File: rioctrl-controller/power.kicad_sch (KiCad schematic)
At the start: 60 parts, among them J1 TERM-BLK-2H, U1 TD6811, U2 TPS54335ADDAR, U3 TPS54335ADDAR, U4 NCP114ASN250T1G

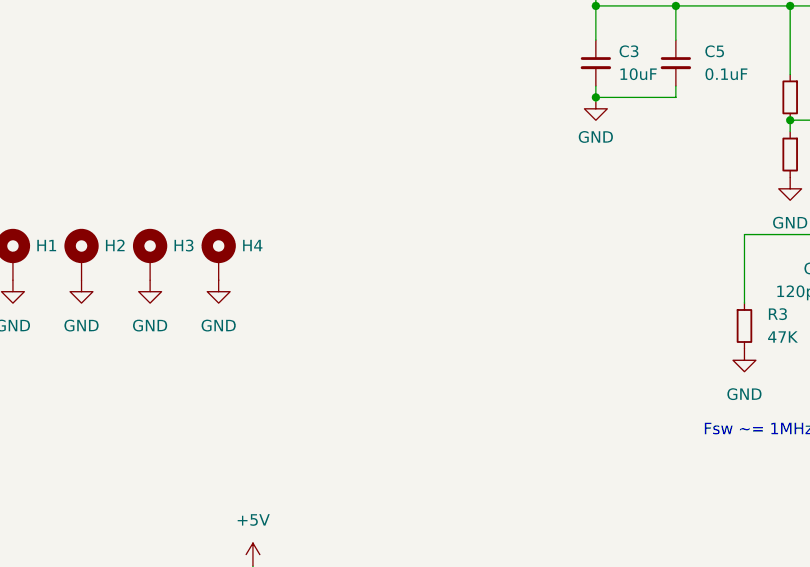
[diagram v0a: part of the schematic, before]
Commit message: Ditch the separate backplane board, increase the slot bitwidth to 12
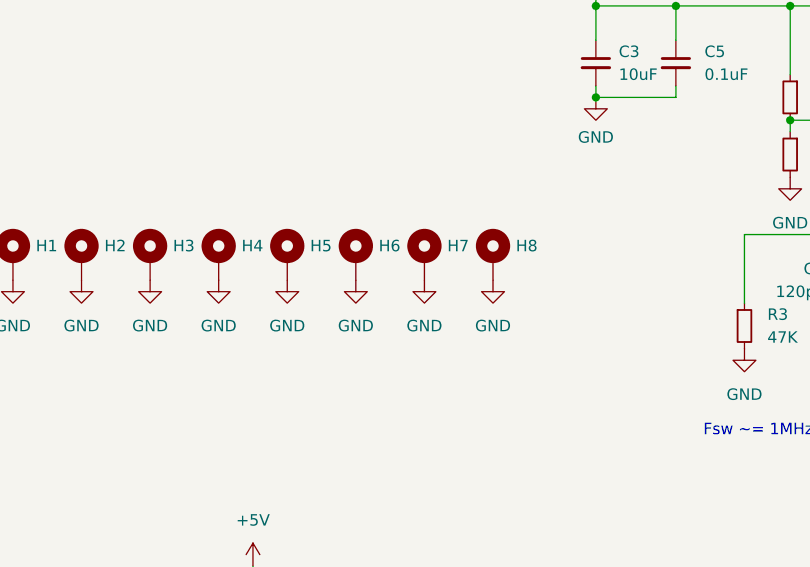
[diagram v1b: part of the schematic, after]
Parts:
- added H5, H6, H7, H8: MH_3.2mm, MountingHole:MountingHole_3.2mm_M3_Pad_Via, symbol hadv-mechanical:MH_3.2mm
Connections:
- net GND: now also H5.1, H6.1, H7.1, H8.1

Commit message: Fix ERC, add title information to sch, add initial version of build scripts
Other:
- company: (none) -> R. Veips
- title: (none) -> ${PROJECTNAME}
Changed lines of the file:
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@@
 	(generator_version "8.0")
 	(paper "A4")
+	(title_block
+		(title "${PROJECTNAME}")
+		(date "2024-08-25")
+		(rev "${VERSION}")
+		(company "R. Veips")
+	)
 	(junction
 		(at 45.72 29.21)

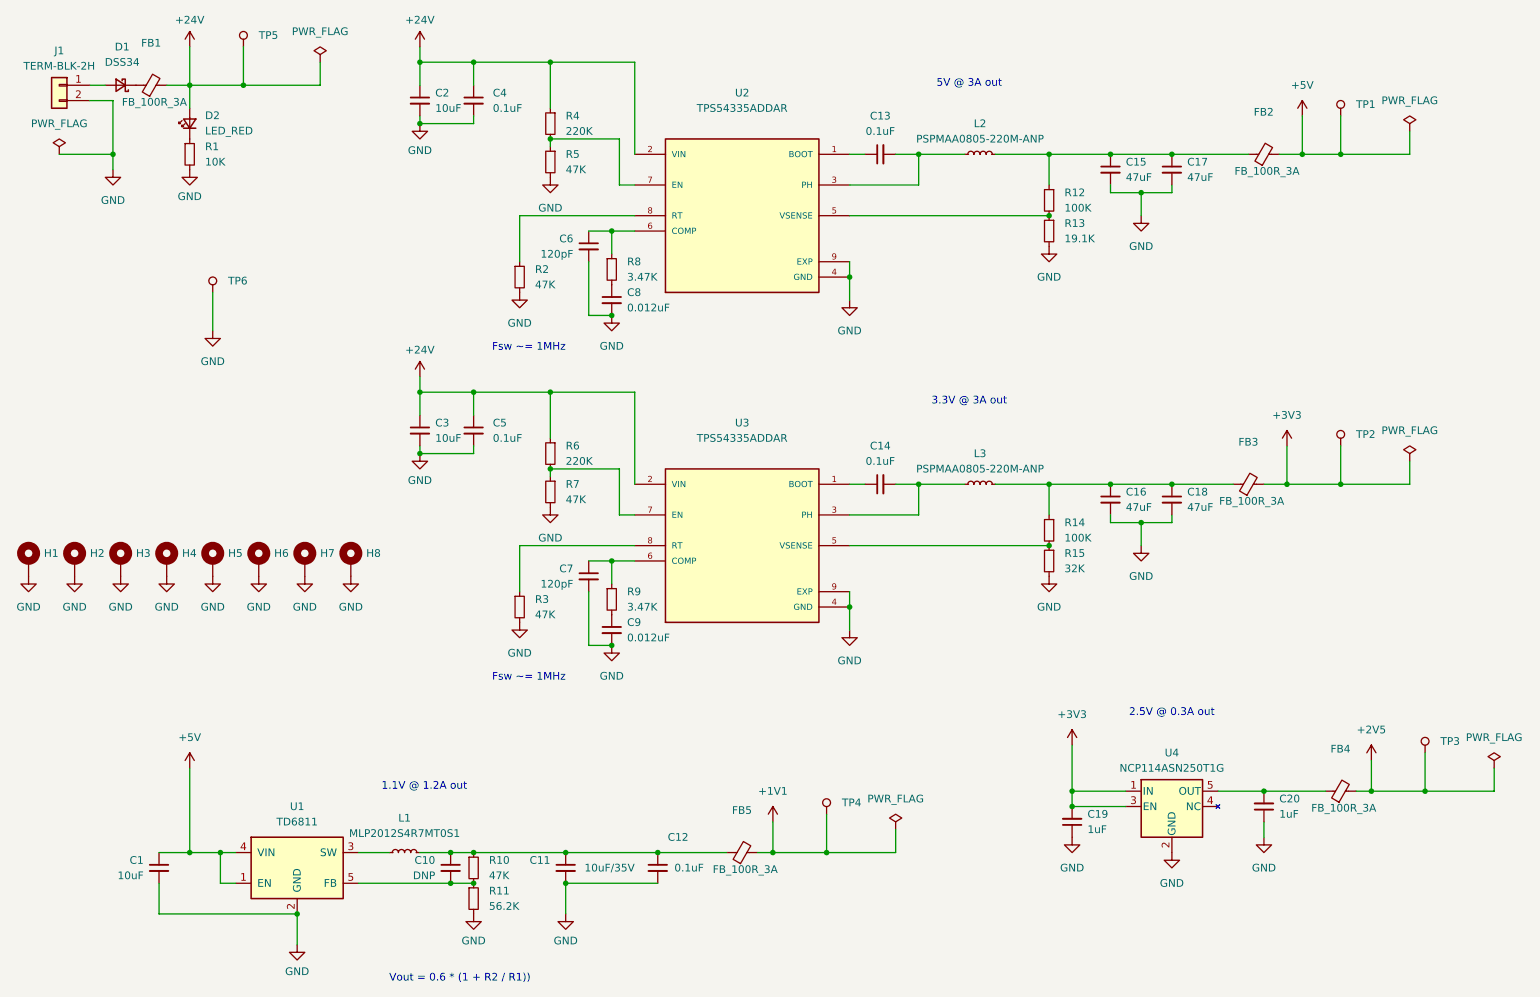
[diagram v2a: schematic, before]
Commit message: Fill in BOM (LCSC#)
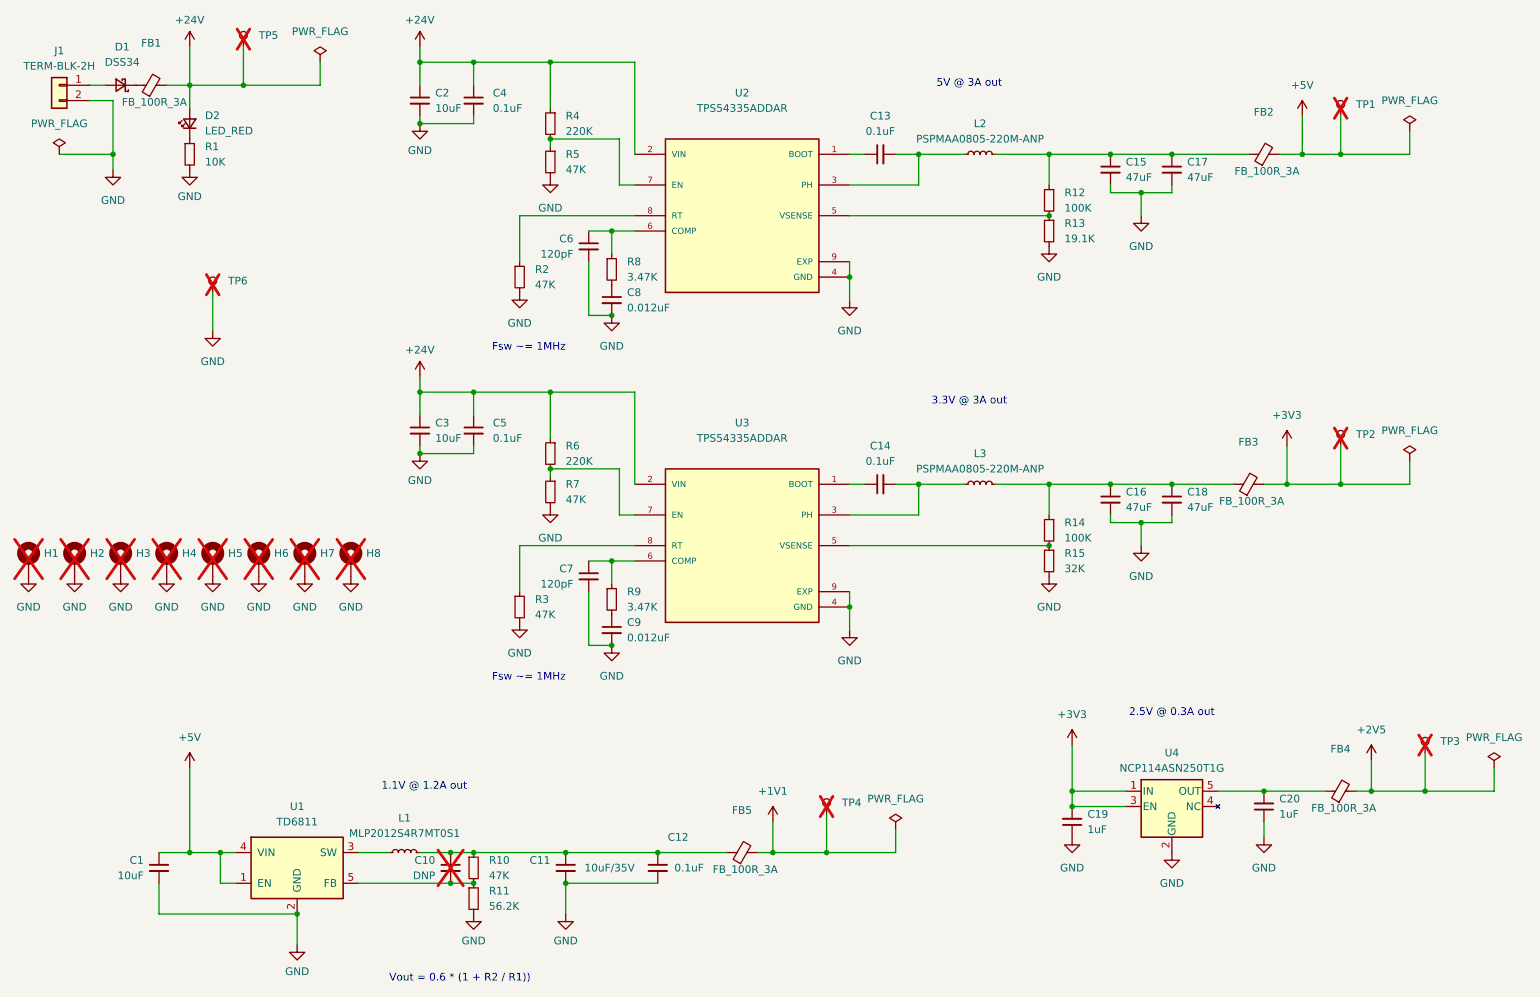
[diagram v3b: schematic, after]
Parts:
- C1, C11: LCSC# C361063 -> C440198
- C10, H1, H2, H3, H4, H5, H6, H7, H8, TP1, TP2, TP3, TP4, TP5, TP6: now not fitted
- C13, C14, C4, C5: LCSC# (none) -> C14663
- C15, C16, C17, C18: LCSC# C440198 -> C6119904
- C19, C20: LCSC# (none) -> C5673
- C6, C7: LCSC# (none) -> C107035
- C8, C9: LCSC# (none) -> C282672
- R1: LCSC# (none) -> C98220
- R10, R2, R3, R5, R7: LCSC# (none) -> C105579
- R12, R14: LCSC# (none) -> C112314
- R13: LCSC# (none) -> C173754
- R15: LCSC# (none) -> C861839
- R4, R6: LCSC# (none) -> C123420
- R8, R9: LCSC# (none) -> C273778

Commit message: fix LCSC part number and MPN for R11 and R26
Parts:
- R11: LCSC# C98220 -> C2930117; MPN RC0603FR-0710KL -> FRC0603F5622TS
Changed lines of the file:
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@@
 			)
 		)
-		(property "LCSC#" "C98220"
+		(property "LCSC#" "C2930117"
 			(at 92.71 163.83 0)
 			(effects
@@
 			)
 		)
-		(property "MPN" "RC0603FR-0710KL"
+		(property "MPN" "FRC0603F5622TS"
 			(at 92.71 163.83 0)
 			(effects
